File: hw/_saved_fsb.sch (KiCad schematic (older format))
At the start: 11 parts, among them J101 AMPSEAL_8_POS_VERT_WHITE_SEAL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, J102 AMPSEAL_23_POS_VERT_WHITE_SEA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

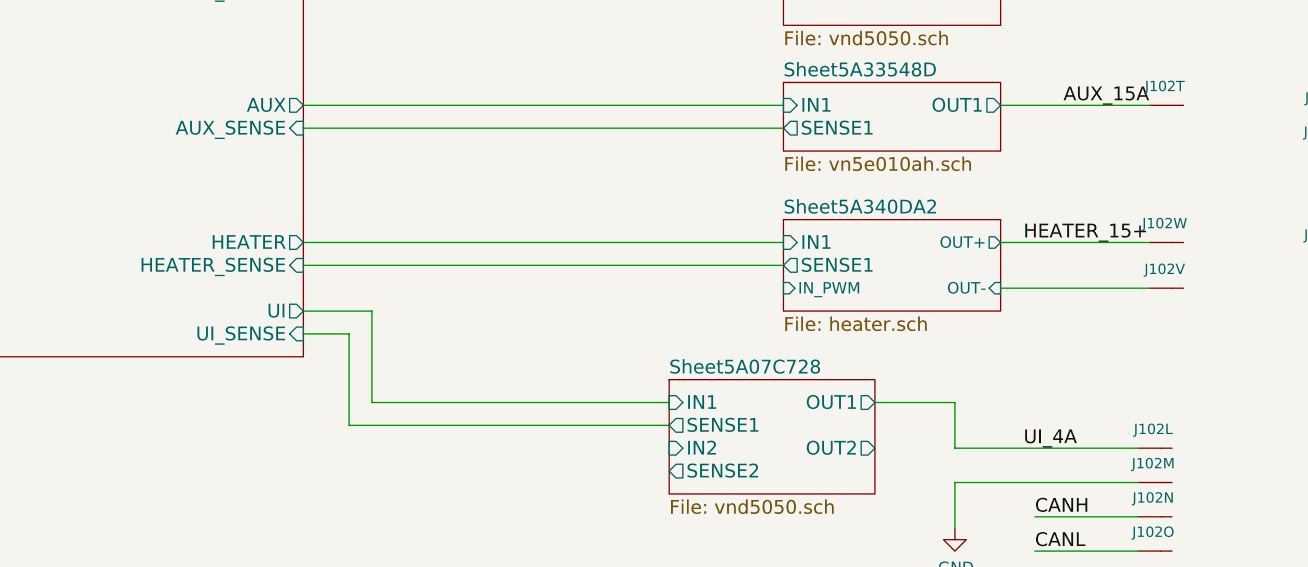
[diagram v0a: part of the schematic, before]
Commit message: 3.0.0 hw with low side heater mosfet
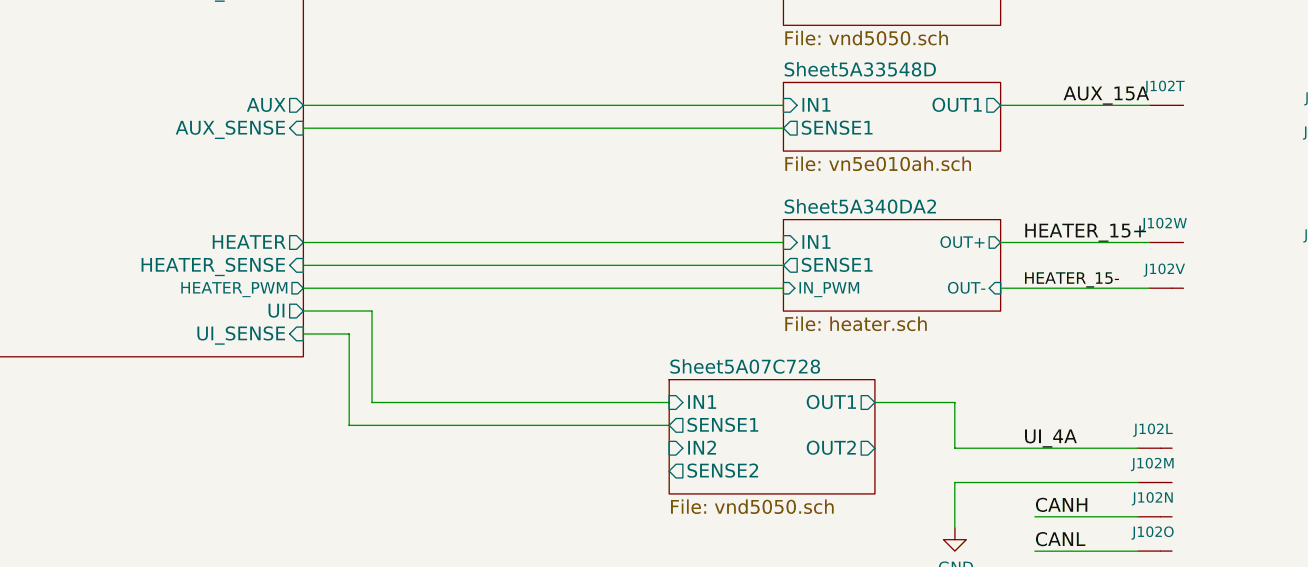
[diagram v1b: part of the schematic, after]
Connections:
- net Sheet5A340DA2/OUT- renamed HEATER_15-
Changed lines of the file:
@@
 $EndSheet
 $Comp
-L fsb-rescue:VDD #PWR101
+L fsb-rescue:VDD #PWR0101
 U 1 1 59541057
 P 3450 1150
-F 0 "#PWR101" H 3450 1000 50  0001 C CNN
+F 0 "#PWR0101" H 3450 1000 50  0001 C CNN
 F 1 "VDD" H 3467 1323 50  0000 C CNN
 F 2 "" H 3450 1150 50  0000 C CNN
@@
 $EndComp
 $Comp
-L fsb-rescue:+5V #PWR102
+L fsb-rescue:+5V #PWR0102
 U 1 1 595410AC
 P 3650 1150
-F 0 "#PWR102" H 3650 1000 50  0001 C CNN
+F 0 "#PWR0102" H 3650 1000 50  0001 C CNN
 F 1 "+5V" H 3665 1323 50  0000 C CNN
 F 2 "" H 3650 1150 50  0000 C CNN
@@
 $EndComp
 $Comp
-L fsb-rescue:+3V3 #PWR103
+L fsb-rescue:+3V3 #PWR0103
 U 1 1 595410EA
 P 3850 1150
-F 0 "#PWR103" H 3850 1000 50  0001 C CNN
+F 0 "#PWR0103" H 3850 1000 50  0001 C CNN
 F 1 "+3V3" H 3865 1323 50  0000 C CNN
 F 2 "" H 3850 1150 50  0000 C CNN
@@
 F21 "DOORSW2" I L 4250 5050 60
 F22 "SEATSW" I L 4250 4700 60
+F23 "HEATER_PWM" O R 6400 5200 50
 $EndSheet
 $Comp
@@
 RADIO_4A
 $Comp
-L fsb-rescue:+BATT #PWR104
+L fsb-rescue:+BATT #PWR0104
 U 1 1 598A906F
 P 8350 1900
-F 0 "#PWR104" H 8350 1750 50  0001 C CNN
+F 0 "#PWR0104" H 8350 1750 50  0001 C CNN
 F 1 "+BATT" H 8365 2073 50  0000 C CNN
 F 2 "" H 8350 1900 50  0000 C CNN
@@
 KEY_30/B
 $Comp
-L fsb-rescue:VDD #PWR105
+L fsb-rescue:VDD #PWR0105
 U 1 1 598AABFA
 P 8500 1150
-F 0 "#PWR105" H 8500 1000 50  0001 C CNN
+F 0 "#PWR0105" H 8500 1000 50  0001 C CNN
 F 1 "VDD" H 8517 1323 50  0000 C CNN
 F 2 "" H 8500 1150 50  0000 C CNN
@@
 	9250 6050 9250 6250
 $Comp
-L fsb-rescue:GND #PWR106
+L fsb-rescue:GND #PWR0106
 U 1 1 5A07BF1C
 P 9250 6250
-F 0 "#PWR106" H 9250 6000 50  0001 C CNN
+F 0 "#PWR0106" H 9250 6000 50  0001 C CNN
 F 1 "GND" H 9255 6077 50  0000 C CNN
 F 2 "" H 9250 6250 50  0000 C CNN
@@
 Wire Wire Line
 	10100 5200 9450 5200
+Text Label 9550 5200 0    50   ~ 0
+HEATER_15-
+Wire Wire Line
+	6400 5200 8500 5200
 $EndSCHEMATC
